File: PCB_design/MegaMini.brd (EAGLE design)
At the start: 47.9 x 53.3 mm, 26 parts, among them IC1 2560-16AU, IC2 DS1307, J1 AVR_SPI_PROG_3X2NS, Y1 16MHz, Y2 32.768KHz

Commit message: Added silkscreen, finished design.
Everything is finished, generating gerber files for the board house.
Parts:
- added U$1: (no value), SparkFun-Aesthetics:OSHW-LOGO-L
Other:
- board size 47.9 x 53.3 mm -> 53 x 58.4 mm
- board text added: "GND"
- board text added: "MegaMini_RTC revision 1.0"
- board text added: "PA3"
- board text added: "PA4"
- board text added: "PA5"
- board text added: "PA6"
- board text added: "PA7"
- board text added: "PB4"
- board text added: "PB5"
- board text added: "PB6"
- board text added: "PB7"
- board text added: "PC0"
- board text added: "PC1"
- board text added: "PC2"
- board text added: "PC3"
- board text added: "PC4"
- board text added: "PC5"
- board text added: "PC6"
- board text added: "PC7"
- board text added: "PD0"
- board text added: "PD1"
- board text added: "PD7"
- board text added: "PE3"
- board text added: "PE5"
- board text added: "PG0"
- board text added: "PG1"
- board text added: "PG2"
- board text added: "PG5"
- board text added: "PH3"
- board text added: "PH4"
- board text added: "PH5"
- board text added: "PH6"
- board text added: "PL0"
- board text added: "PL1"
- board text added: "PL2"
- board text added: "PL3"
- board text added: "PL4"
- board text added: "PL5"
- board text added: "PL6"
- board text added: "PL7"
- board text added: "RST"
- board text added: "RX0"
- board text added: "TX0"
- board text added: "VCC"

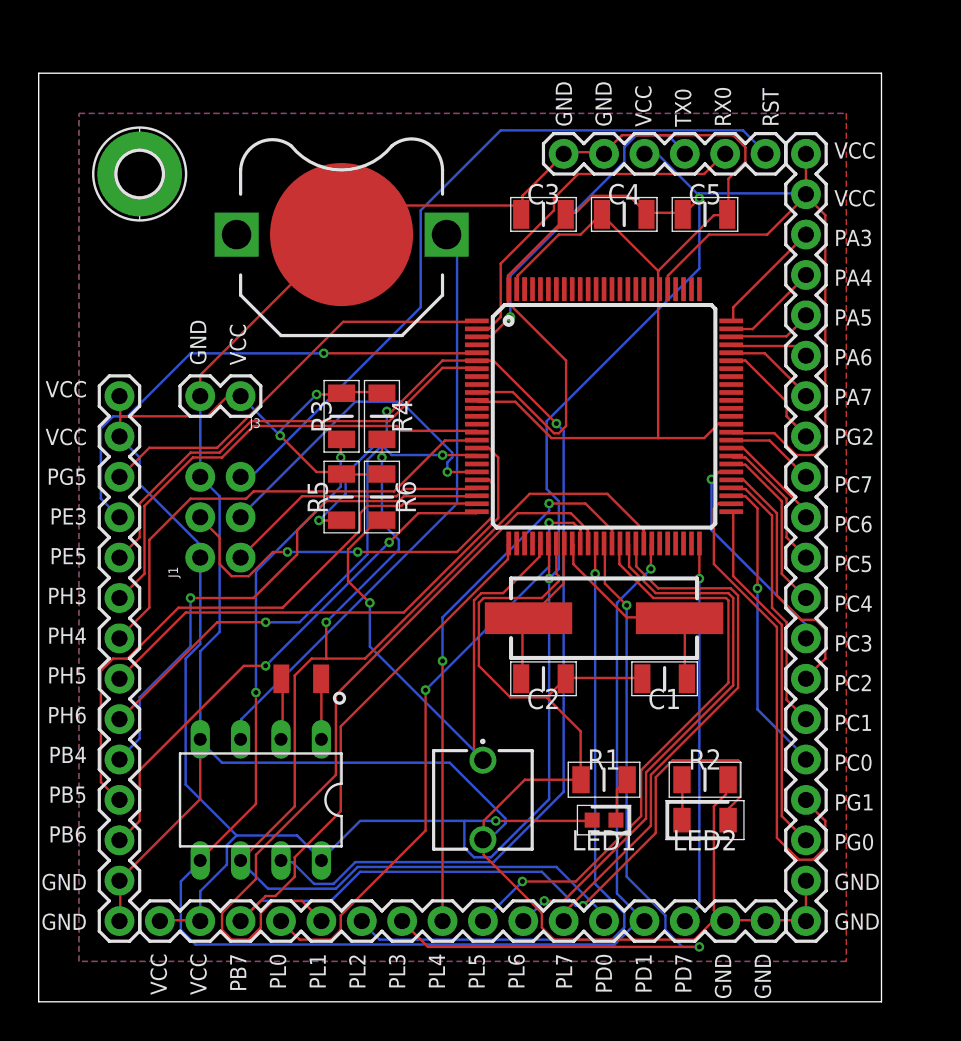
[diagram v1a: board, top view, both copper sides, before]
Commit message: Some small adjustements to the 3D print
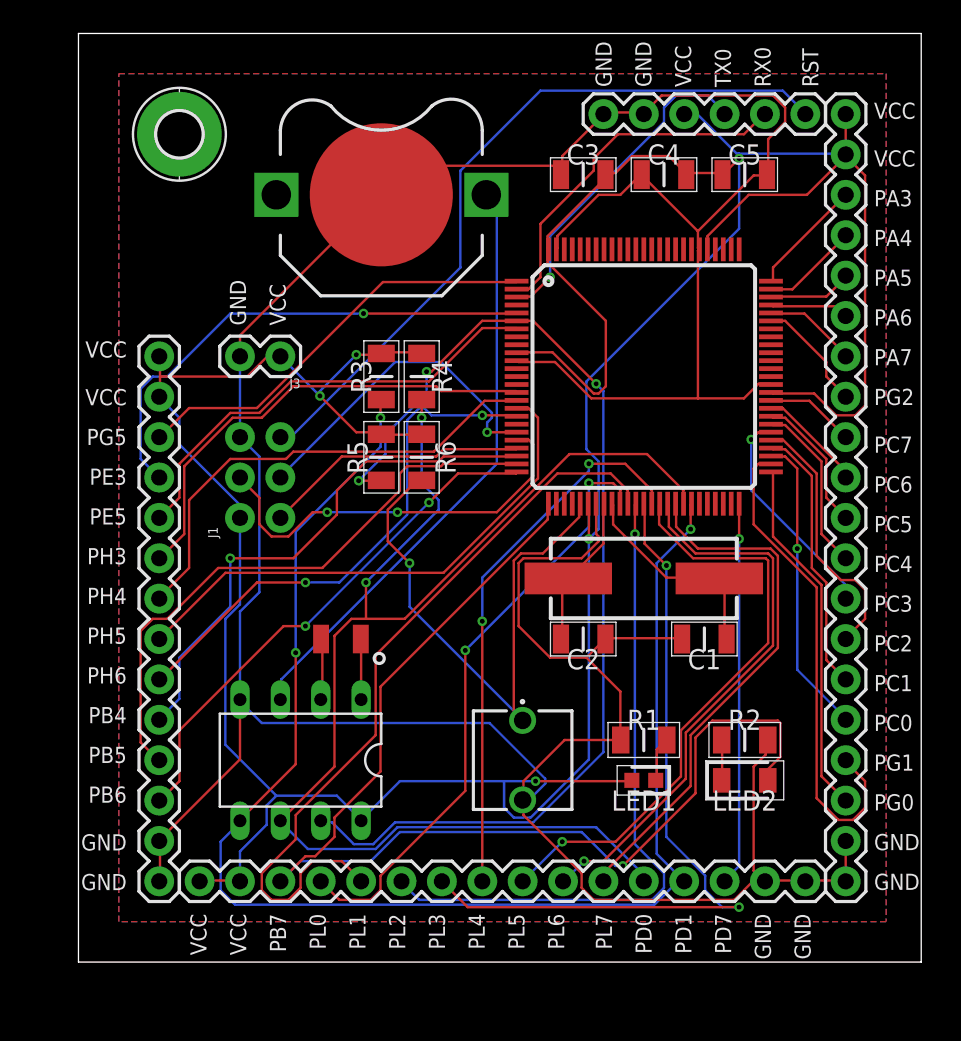
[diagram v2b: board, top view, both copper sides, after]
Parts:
- moved BT1 3.54 mm to (19.0, 48.2)
- moved C1 3.54 mm to (39.3, 20.3)
- moved C2 3.54 mm to (31.7, 20.3)
- moved C3 3.54 mm to (31.7, 49.5)
- moved C4 3.54 mm to (36.8, 49.5)
- moved C5 3.54 mm to (41.9, 49.5)
- moved IC1 3.54 mm to (35.5, 36.8)
- moved IC2 3.54 mm to (13.9, 12.7)
- moved J1 3.54 mm to (11.4, 30.4)
- moved J2 3.54 mm to (45.7, 53.3)
- moved J3 3.54 mm to (12.7, 38.1)
- moved J4 3.54 mm to (7.58, 5.04)
- moved J5 3.54 mm to (5.04, 5.04)
- moved J6 3.54 mm to (48.2, 53.3)
- moved LED1 3.54 mm to (35.5, 11.4)
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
